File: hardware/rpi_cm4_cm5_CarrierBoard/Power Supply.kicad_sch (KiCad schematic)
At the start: 84 parts, among them Q13 2N7002, Q7 2N7002, Q8 2N7002, U10 TPS54527DDAR, U11 TPS54527DDAR, U12 TPS7A7001DDAR, U13 SE555DR, U14 SN74LVC1G14DBVR, U9 TPS54527DDAR

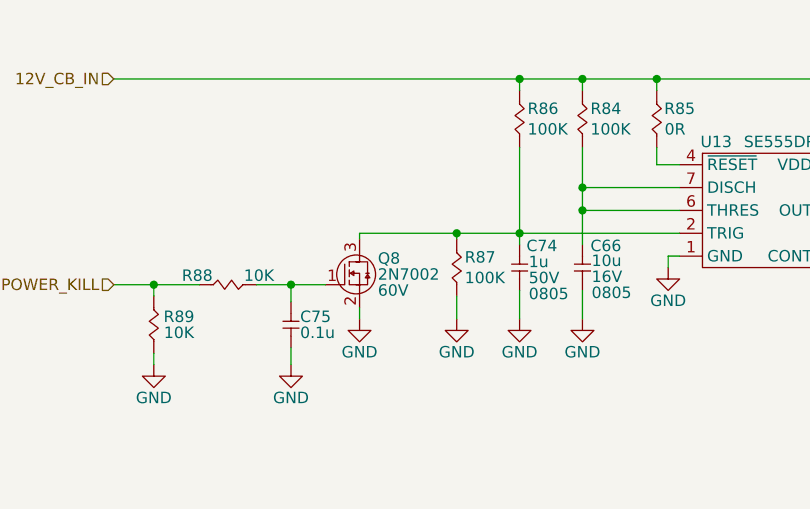
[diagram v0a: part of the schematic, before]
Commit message: Add power-up and power kill sequences Modify schematics to add net classes for DiffPairs
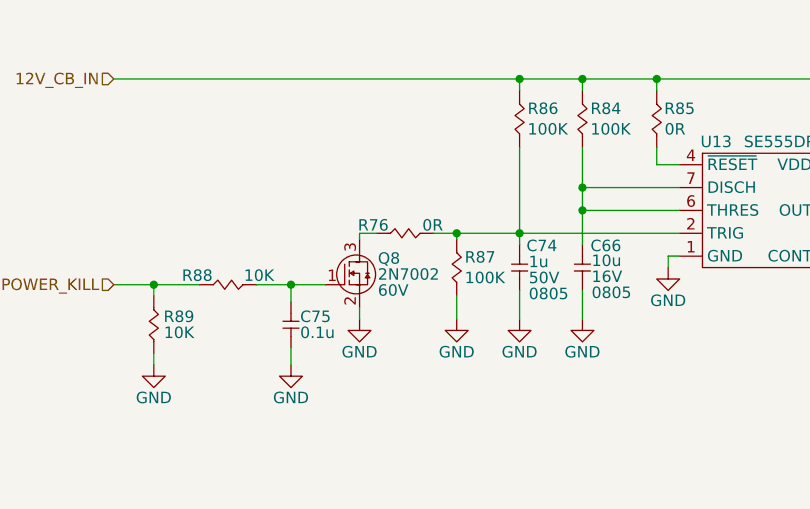
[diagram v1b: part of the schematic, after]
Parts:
- added R76: 0R, footprint:RES_0402, symbol KicadCompDb:Resistors/RES_SMT_00001
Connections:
- net at C74.2, R86.1, R87.2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: now also R76.2; no longer Q8.3 (D)
- new net: Q8.3 (D), R76.1
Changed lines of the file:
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@@
 	)
 	(junction
-		(at 65.405 37.465)
-		(diameter 0)
-		(color 0 0 0 0)
-	)
-	(junction
 		(at 247.65 101.6)
 		(diameter 0)
@@
 	)
 	(junction
+		(at 65.405 37.465)
+		(diameter 0)
+		(color 0 0 0 0)
+	)
+	(junction
 		(at 247.015 71.755)
 		(diameter 0)
@@
 	(wire
 		(pts
-			(xy 54.61 37.465) (xy 65.405 37.465)
-		)
-		(stroke
-			(width 0)
-			(type default)
-		)
-	)
-	(wire
-		(pts
 			(xy 267.335 59.69) (xy 267.335 60.96)
 		)
@@
 	(wire
 		(pts
+			(xy 62.865 37.465) (xy 65.405 37.465)
+		)
+		(stroke
+			(width 0)
+			(type default)
+		)
+	)
+	(wire
+		(pts
 			(xy 260.35 71.755) (xy 254 71.755)
 		)
@@
 	(wire
 		(pts
+			(xy 54.61 37.465) (xy 56.515 37.465)
+		)
+		(stroke
+			(width 0)
+			(type default)
+		)
+	)
+	(wire
+		(pts
 			(xy 172.085 20.32) (xy 172.085 21.59)
 		)
@@
 					(unit 1)
 				)
+			)
+		)
+	)
+	(symbol
+		(lib_id "KicadCompDb:Resistors/RES_SMT_00001")
+		(at 57.785 37.465 0)
+		(unit 1)
+		(exclude_from_sim no)
+		(in_bom yes)
+		(on_board yes)
+		(dnp no)
+		(property "Reference" "R76"
+			(at 56.134 36.576 0)
+			(effects
+				(font
+					(size 1.27 1.27)
+				)
+			)
+		)
+		(property "Value" "0R"
+			(at 62.738 36.576 0)
+			(effects
+				(font
+					(size 1.27 1.27)
+				)
+			)
+		)
+		(property "Footprint" "footprint:RES_0402"
+			(at 58.293 59.563 0)
+			(effects
+				(font
+					(size 1.27 1.27)
+				)
+				(hide yes)
+			)
+		)
+		(property "Datasheet" "https://www.yageogroup.com/content/datasheet/asset/file/PYU-RC_GROUP_51_ROHS_L"
+			(at 57.785 37.465 0)
+			(effects
+				(font
+					(size 1.27 1.27)
+				)
+				(hide yes)
+			)
+		)
+		(property "Description" "RES 0 OHM JUMPER 1/16W 0402"
+			(at 59.563 47.371 0)
+			(effects
+				(font
+					(size 1.27 1.27)
+				)
+				(hide yes)
+			)
+		)
+		(property "Tolerance" "1%"
+			(at 58.039 57.785 0)
+			(effects
+				(font
+					(size 1.27 1.27)
+				)
+				(hide yes)
+			)
+		)
+		(property "Power" "1/16W"
+			(at 58.039 51.689 0)
+			(effects
+				(font
+					(size 1.27 1.27)
+				)
+				(hide yes)
+			)
+		)
+		(property "Package" "0402"
+			(at 57.785 53.721 0)
+			(effects
+				(font
+					(size 1.27 1.27)
+				)
+				(hide yes)
+			)
+		)
+		(property "Manufacturer" "YAGEO"
+			(at 58.039 55.753 0)
+			(effects
+				(font
+					(size 1.27 1.27)
+				)
+				(hide yes)
+			)
+		)
+		(property "Manufacturer Part Number" "RC0402FR-071KL"
+			(at 58.039 45.339 0)
+			(effects
+				(font
+					(size 1.27 1.27)
+				)
+				(hide yes)
+			)
+		)
+		(property "Distributor" "DigiKey"
+			(at 57.785 43.307 0)
+			(effects
+				(font
+					(size 1.27 1.27)
+				)
+				(hide yes)
+			)
+		)
+		(property "Distributor Part Number" "311-0.0JRCT-ND"
+			(at 58.547 49.657 0)
+			(effects
+				(font
+					(size 1.27 1.27)
+				)
+				(hide yes)
+			)
+		)
+		(property "Temperature Coefficient" "±100ppm/°C"
+			(at 57.785 37.465 0)
+			(effects
+				(font
+					(size 1.27 1.27)
+				)
+				(hide yes)
+			)
+		)
+		(property "Operating Temperature" "-55°C ~ 155°C"
+			(at 58.547 61.849 0)
+			(effects
+				(font
+					(size 1.27 1.27)
+				)
+				(hide yes)
+			)
+		)
+		(property "Type" "RES SMT"
+			(at 57.785 37.465 0)
+			(show_name yes)
+			(effects
+				(font
+					(size 1.27 1.27)
+				)
+				(hide yes)
+			)
+		)
+		(property "Dimensions" "1.00mm x 0.50mm"
+			(at 57.785 37.465 0)
+			(show_name yes)
+			(effects
+				(font
+					(size 1.27 1.27)
+				)
+				(hide yes)
+			)
+		)
+		(pin "1"
+		)
+		(pin "2"
+		)
+		(instances
+			(project "rpi_cm4_cm5_CarrierBoard"
+				(path "/7dcdf741-90ca-4333-848c-806f4d64158e/e2b15d84-0407-4e36-9277-ffea8d1dbee5"
+					(reference "R76")
+					(unit 1)
+				)

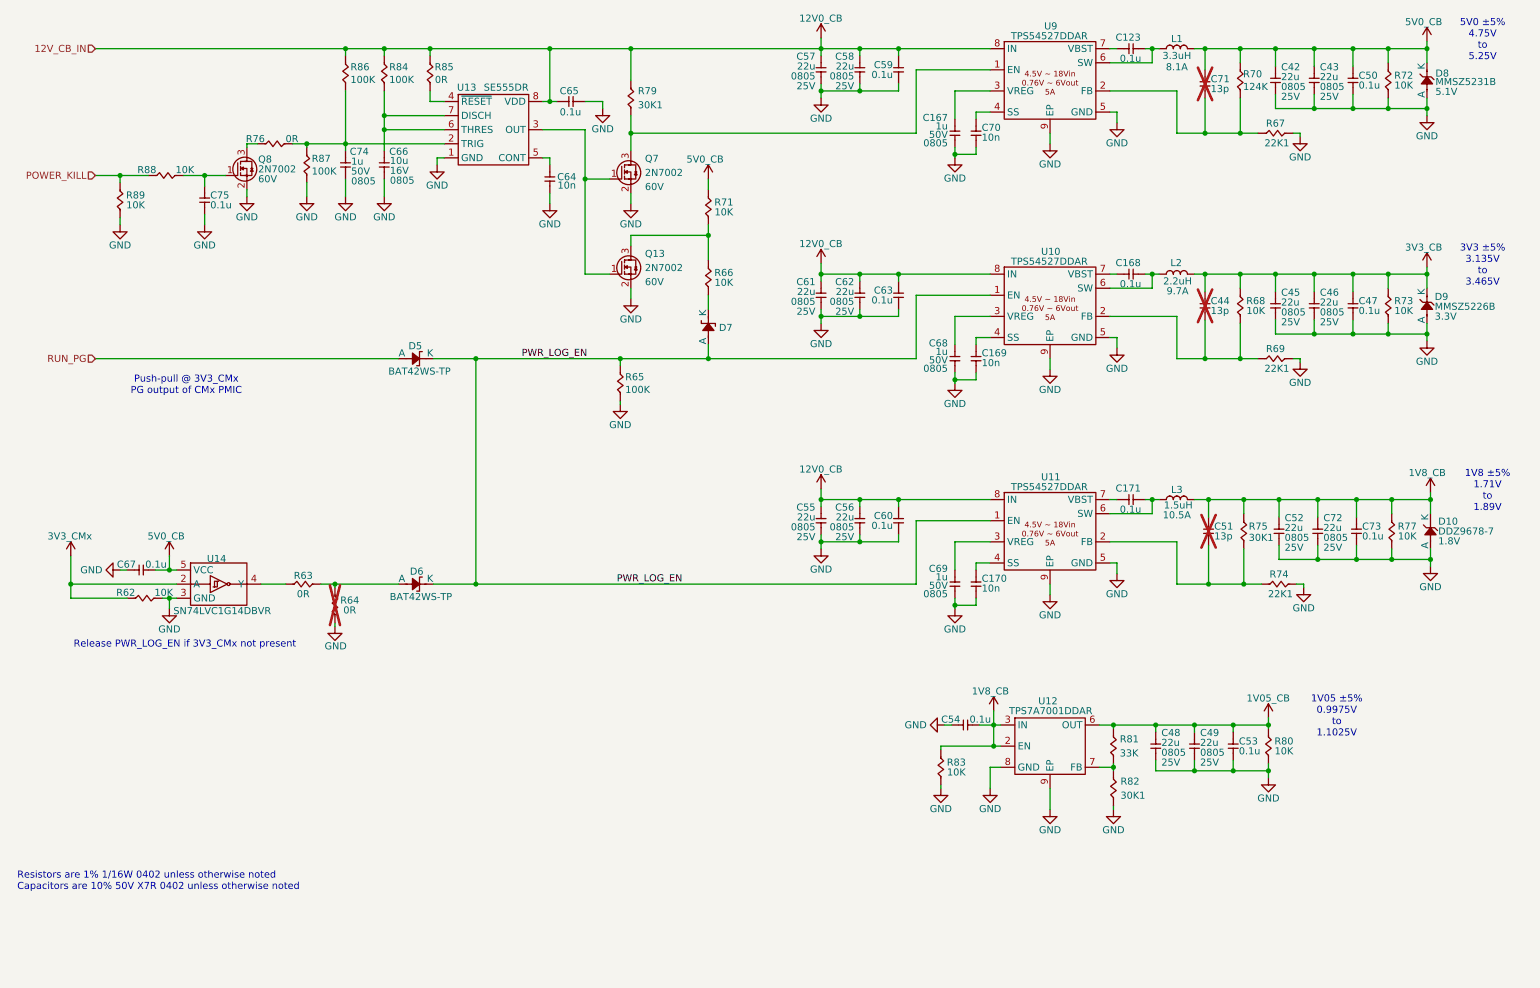
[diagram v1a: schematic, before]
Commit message: Significant update to schematics Add codec, Mikrobus, PIC32A Add power table, design notes for pinmux Add datasheets
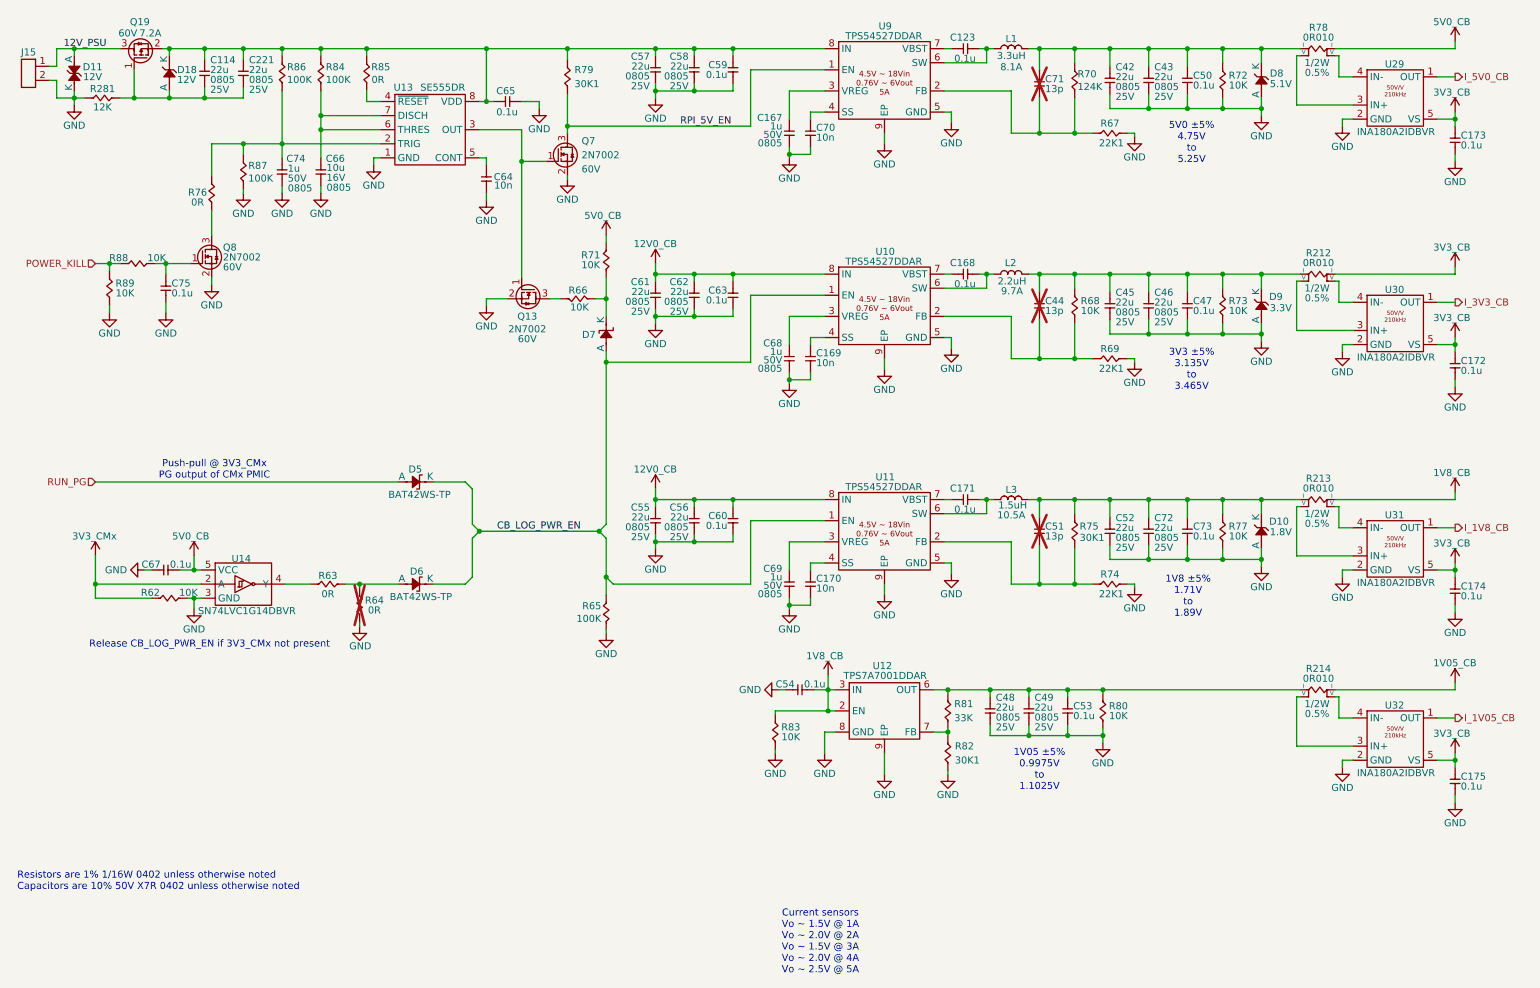
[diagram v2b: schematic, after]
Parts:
- added C114, C221: 22u, footprint:CAP_NONPOL_0805, symbol KicadCompDb:Capacitors/CAP_CER_SMT_00011
- added C172, C173, C174, C175: 0.1u, footprint:CAP_NONPOL_0402, symbol KicadCompDb:Capacitors/CAP_CER_SMT_00001
- added D11: SMAJ12CA, footprint:DO-214AC, symbol KicadCompDb:ESD Diodes/ESD_DIODE_00005
- added D18: MMSZ5242B-TP, footprint:SOD-123, symbol KicadCompDb:Diodes/DIODE_00003
- added J15: TB002-500-02BE, footprint:TB002-500-02BE, symbol KicadCompDb:Connector/CONN_00018
- added Q19: DMPH6050SK3-13, footprint:TO-252-3, symbol KicadCompDb:Mosfet/MOSFET_00003
- added R212, R213, R214, R78: 0R010, footprint:RES_SENSE_1206, symbol KicadCompDb:Resistors/RES_SMT_00033
- added R281: 12K, footprint:RES_0402, symbol KicadCompDb:Resistors/RES_SMT_00014
- added U29, U30, U31, U32: INA180A2IDBVR, footprint:SOT-23-5, symbol KicadCompDb:Amplifier/AMP_00001
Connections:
- net 12V0_CB: no longer C57.2, C58.2, C59.2, C65.2, R79.2, R84.2, R85.2, R86.2, U13.8 (VDD), U9.8 (IN)
- net 1V05_CB: now also R214.4 (I); no longer C48.2, C49.2, C53.2, R80.2, R81.2, U12.6 (OUT)
- net 1V8_CB: now also R213.4 (I); no longer C51.2, C52.2, C72.2, C73.2, D10.1 (K), L3.2, R75.2, R77.2
- net 3V3_CB: now also C172.2, C173.2, C174.2, C175.2, R212.4 (I), U29.5 (VS), U30.5 (VS), U31.5 (VS), U32.5 (VS); no longer C44.2, C45.2, C46.2, C47.2, D9.1 (K), L2.2, R68.2, R73.2
- net 5V0_CB: now also R78.4 (I); no longer C42.2, C43.2, C50.2, C71.2, D8.1 (K), L1.2, R70.2, R72.2
- net GND: now also C172.1, C173.1, C174.1, C175.1, D11.1 (K), J15.2, R281.1, U29.2 (GND), U30.2 (GND), U31.2 (GND), U32.2 (GND)
- net at D7.1 (K), R66.1: now also R71.1
- net at Q13.3 (D), R66.2: no longer R71.1
- net RPI_5V_EN: now reaches Q7.3 (D), R79.1, U9.1 (EN)
- net PWR_LOG_EN renamed CB_LOG_PWR_EN
- new net: C114.2, C221.2, C57.2, C58.2, C59.2, C65.2, D18.1 (K), Q19.2 (S), R79.2, R84.2, R85.2, R86.2, U13.8 (VDD), U9.8 (IN)
- new net: R214.2 (V), U32.3 (IN+)
- new net: R214.3 (V), U32.4 (IN-)
- new net: C114.1, C221.1, D18.2 (A), Q19.1 (G), R281.2
- new net: C51.2, C52.2, C72.2, C73.2, D10.1 (K), L3.2, R213.1 (I), R75.2, R77.2
- new net: R213.2 (V), U31.3 (IN+)
- new net: R213.3 (V), U31.4 (IN-)
- new net: C48.2, C49.2, C53.2, R214.1 (I), R80.2, R81.2, U12.6 (OUT)
- new net: C42.2, C43.2, C50.2, C71.2, D8.1 (K), L1.2, R70.2, R72.2, R78.1 (I)
- new net: R78.2 (V), U29.3 (IN+)
- new net: R78.3 (V), U29.4 (IN-)
- new net: C44.2, C45.2, C46.2, C47.2, D9.1 (K), L2.2, R212.1 (I), R68.2, R73.2
- new net: R212.2 (V), U30.3 (IN+)
- new net: R212.3 (V), U30.4 (IN-)
- new net 12V_PSU: D11.2 (A), J15.1, Q19.3 (D)
- new net I_1V05_CB: U32.1 (OUT)
- new net I_1V8_CB: U31.1 (OUT)
- new net I_3V3_CB: U30.1 (OUT)
- new net I_5V0_CB: U29.1 (OUT)
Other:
- note added: "Current sensors Vo ~ 1.5V @ 1A Vo ~ 2.0V @ 2A Vo ~ 1.5V @ 3A Vo ~ 2.0V @ 4A Vo ~ 2.5V @ 5A"
- note added: "Release CB_LOG_PWR_EN if 3V3_CMx not present"
- note removed: "Release PWR_LOG_EN if 3V3_CMx not present"
- moved on the sheet: C123, C167, C168, C169, C170, C171, C42, C43, C44, C45, C46, C47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

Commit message: Preliminary completion of RPI CMx schematics Cleaned up hierarchical root page
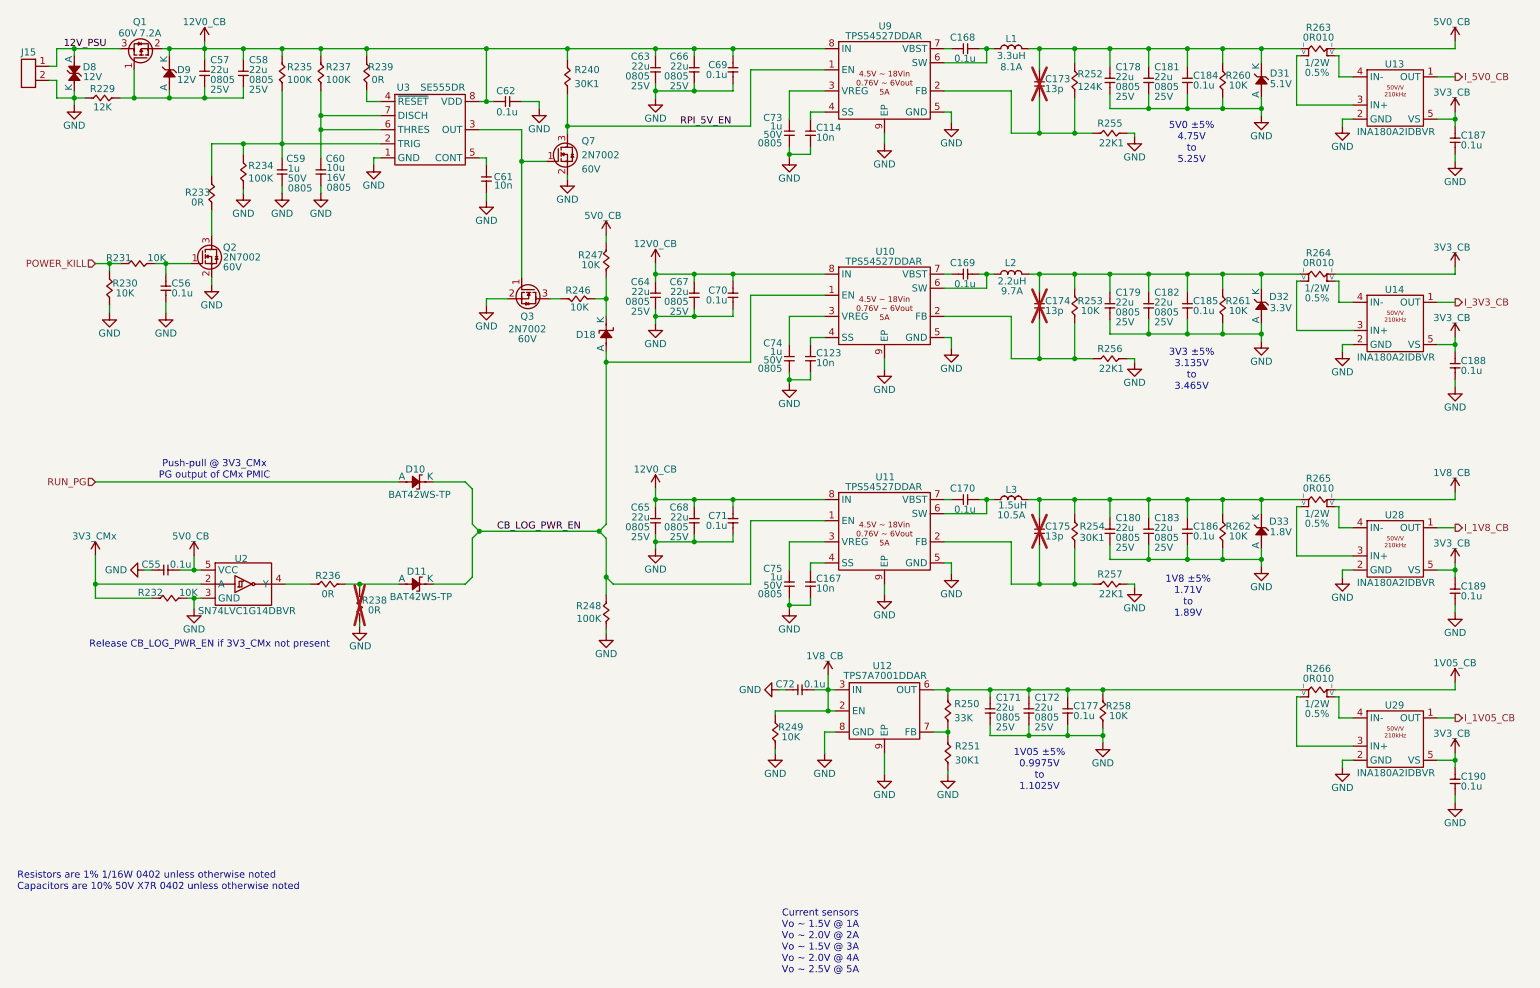
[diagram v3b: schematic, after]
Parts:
- renumbered C70 to C114, C169 to C123, C170 to C167, C123 to C168, C168 to C169, C171 to C170, C48 to C171, C49 to C172, C71 to C173, C44 to C174, C51 to C175, C53 to C177, C42 to C178, C45 to C179, C52 to C180, C43 to C181, C46 to C182, C72 to C183, C50 to C184, C47 to C185, C73 to C186, C173 to C187, C172 to C188, C174 to C189, C175 to C190, C67 to C55, C75 to C56, C114 to C57, C221 to C58, C74 to C59, C66 to C60, C64 to C61, C65 to C62, C57 to C63, C61 to C64, C55 to C65, C58 to C66, C62 to C67, C56 to C68, C59 to C69, C63 to C70, C60 to C71, C54 to C72, C167 to C73, C68 to C74, C69 to C75, D5 to D10, D6 to D11, D7 to D18, D8 to D31, D9 to D32, D10 to D33, D11 to D8, D18 to D9, Q19 to Q1, Q8 to Q2, Q13 to Q3, R281 to R229, R89 to R230, R88 to R231, R62 to R232, R76 to R233, R87 to R234, R86 to R235, R63 to R236, R84 to R237, R64 to R238, R85 to R239, R79 to R240, R66 to R246, R71 to R247, R65 to R248, R83 to R249, R81 to R250, R82 to R251, R70 to R252, R68 to R253, R75 to R254, R67 to R255, R69 to R256, R74 to R257, R80 to R258, R72 to R260, R73 to R261, R77 to R262, R78 to R263, R212 to R264, R213 to R265, R214 to R266, U29 to U13, U30 to U14, U14 to U2, U31 to U28, U32 to U29, U13 to U3
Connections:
- net 12V0_CB: now also C57.2, C58.2, C62.2, C63.2, C66.2, C69.2, D9.1 (K), Q1.2 (S), R235.2, R237.2, R239.2, R240.2, U3.8 (VDD), U9.8 (IN)
